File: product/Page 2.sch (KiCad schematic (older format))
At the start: 25 parts, among them J3 Conn_02x05_Odd_Even, Q1 Q_NMOS_GSD, Q2 Q_NMOS_GSD, Q3 Q_NMOS_GSD, SW1 222CMVBAR, SW2 222CMVBAR, U3 ESP32-WROOM-32D, X1 ECS-2520MV

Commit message: Added first revision of programmer board
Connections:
- net labels removed: +5V
- wire segments 98 -> 96
- no-connect marks 19 -> 20
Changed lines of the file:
@@
 Text GLabel 8450 4750 0    50   Input ~ 0
 RESTART
-$Comp
-L Connector_Generic:Conn_02x05_Odd_Even J3
-U 1 1 5DFAE484
-P 5000 6600
-F 0 "J3" H 5050 6925 50  0000 C CNN
-F 1 "Conn_02x05_Odd_Even" H 5050 6926 50  0001 C CNN
-F 2 "Connector_PinSocket_2.54mm:PinSocket_2x05_P2.54mm_Vertical" H 5000 6600 50  0001 C CNN
-F 3 "~" H 5000 6600 50  0001 C CNN
-	1    5000 6600
-	1    0    0    -1
-$EndComp
 Text GLabel 5500 6500 2    50   Input ~ 0
 RX
@@
 L power:GND #PWR0146
 U 1 1 5DFAF37B
-P 4700 6900
-F 0 "#PWR0146" H 4700 6650 50  0001 C CNN
-F 1 "GND" H 4705 6727 50  0000 C CNN
-F 2 "" H 4700 6900 50  0001 C CNN
-F 3 "" H 4700 6900 50  0001 C CNN
-	1    4700 6900
-	1    0    0    -1
-$EndComp
-$Comp
-L power:+5V #PWR0147
-U 1 1 5DFAF73B
-P 4700 6300
-F 0 "#PWR0147" H 4700 6150 50  0001 C CNN
-F 1 "+5V" H 4715 6473 50  0000 C CNN
-F 2 "" H 4700 6300 50  0001 C CNN
-F 3 "" H 4700 6300 50  0001 C CNN
-	1    4700 6300
-	1    0    0    -1
-$EndComp
-Wire Wire Line
-	4800 6400 4700 6400
-Wire Wire Line
-	4700 6400 4700 6300
-Wire Wire Line
-	4800 6800 4700 6800
-Wire Wire Line
-	4700 6800 4700 6900
+P 5400 6900
+F 0 "#PWR0146" H 5400 6650 50  0001 C CNN
+F 1 "GND" H 5405 6727 50  0000 C CNN
+F 2 "" H 5400 6900 50  0001 C CNN
+F 3 "" H 5400 6900 50  0001 C CNN
+	1    5400 6900
+	1    0    0    -1
+$EndComp
+Wire Wire Line
+	5400 6800 5400 6900
 Wire Wire Line
 	5300 6700 5500 6700
@@
 Wire Wire Line
 	5500 6400 5300 6400
-NoConn ~ 5300 6800
 NoConn ~ 4800 6700
 NoConn ~ 4800 6600
@@
 Text GLabel 3850 3200 2    50   Input ~ 0
 CLKEN
+$Comp
+L Connector_Generic:Conn_02x05_Odd_Even J3
+U 1 1 5DFAE484
+P 5000 6600
+F 0 "J3" H 5050 6925 50  0000 C CNN
+F 1 "Conn_02x05_Odd_Even" H 5050 6926 50  0001 C CNN
+F 2 "Connector_PinSocket_2.54mm:PinSocket_2x05_P2.54mm_Vertical" H 5000 6600 50  0001 C CNN
+F 3 "~" H 5000 6600 50  0001 C CNN
+	1    5000 6600
+	1    0    0    -1
+$EndComp
+Wire Wire Line
+	5300 6800 5400 6800
+NoConn ~ 4800 6800
+NoConn ~ 4800 6400
 $EndSCHEMATC

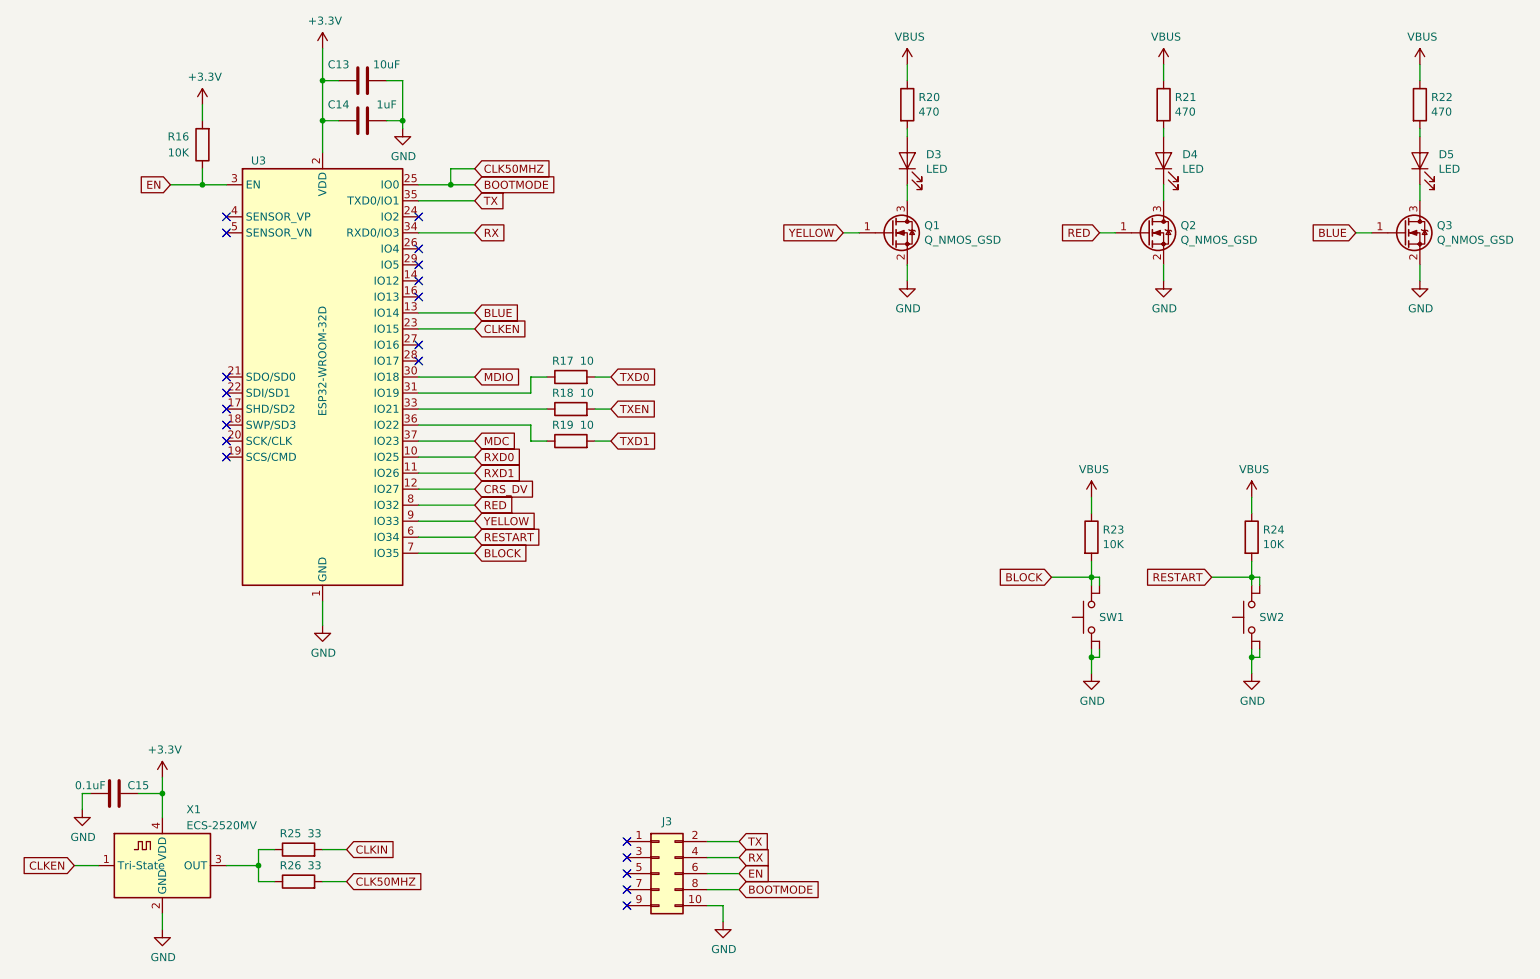
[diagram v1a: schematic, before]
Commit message: Added LCSC part numbers for product board
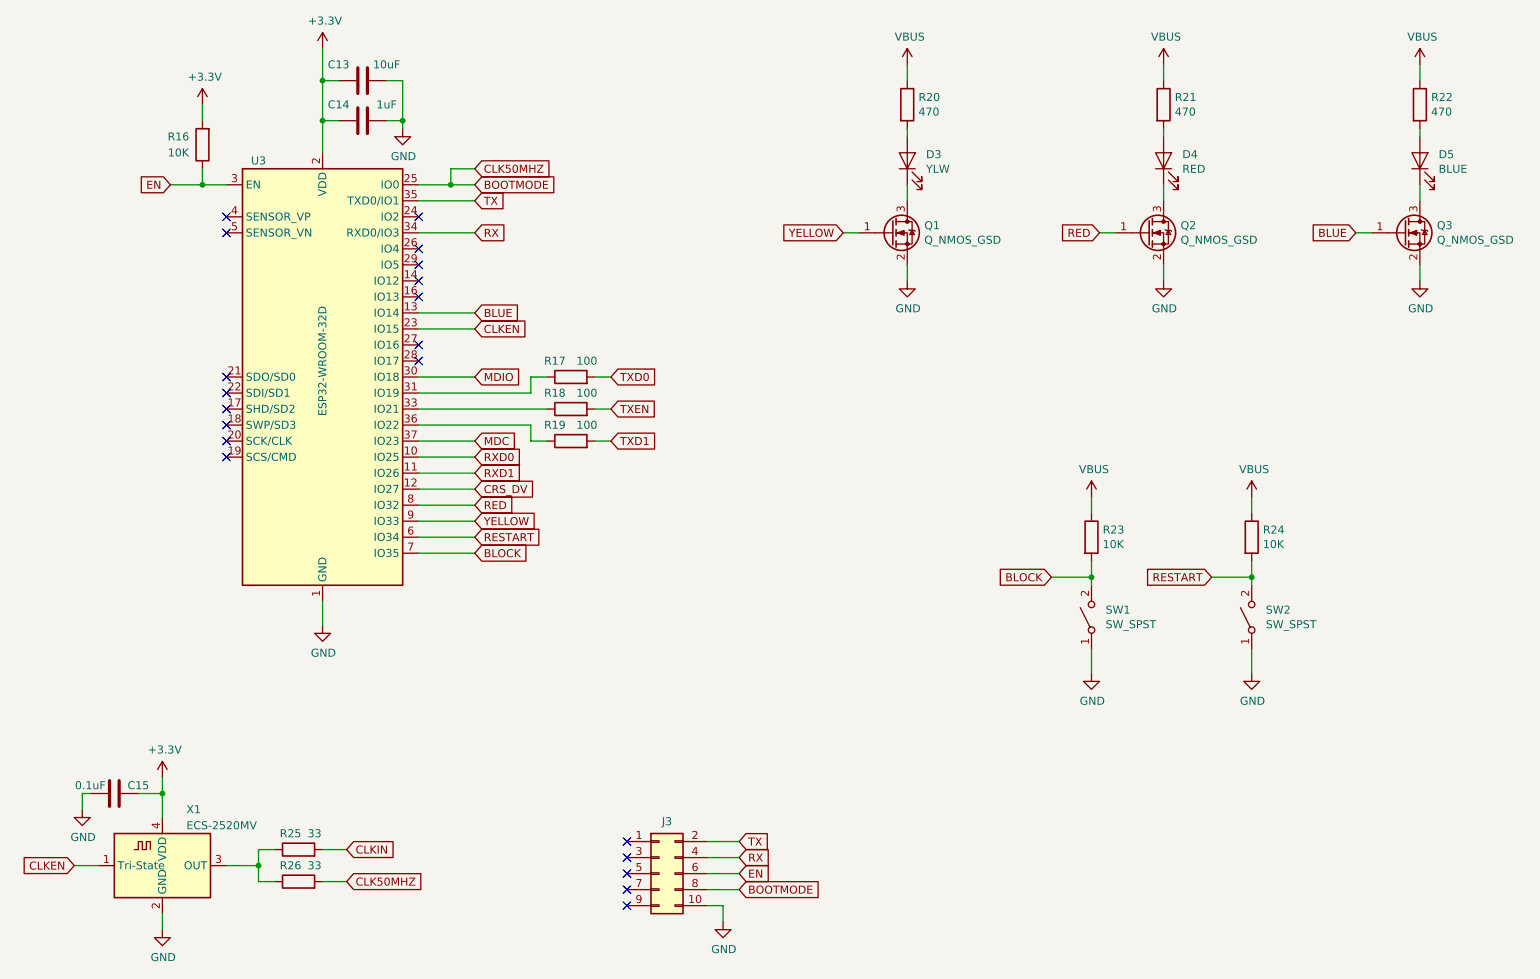
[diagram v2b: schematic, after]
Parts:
- removed SW1, SW2: 222CMVBAR, My Footprints:222CMVBAR, symbol My_Symbols:222CMVBAR
- added SW1, SW2: SW_SPST, Button_Switch_SMD:SW_Push_1P1T_NO_6x6mm_H9.5mm, symbol Switch:SW_SPST
- C13: LCSC Part Number (none) -> C77044
- C14: LCSC Part Number (none) -> C1525
- C15: LCSC Part Number (none) -> C24452
- D3: value LED -> YLW; LCSC Part Number (none) -> C125101
- D4: value LED -> RED; LCSC Part Number (none) -> C125099
- D5: value LED -> BLUE; LCSC Part Number (none) -> C99290
- Q1, Q2, Q3: LCSC Part Number (none) -> C71533
- R16, R23, R24: LCSC Part Number (none) -> C99198
- R17, R18, R19: value 10 -> 100; LCSC Part Number (none) -> C105588
- R20, R21, R22: LCSC Part Number (none) -> C114433
- R25, R26: LCSC Part Number (none) -> C417099
- U3: LCSC Part Number (none) -> C95209
- X1: LCSC Part Number (none) -> C405472
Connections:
- net BLOCK: now also SW1.2 (B)
- net GND: now also SW1.1 (A), SW2.1 (A)
- net RESTART: now also SW2.2 (B)
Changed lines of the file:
@@
 EESchema Schematic File Version 4
-LIBS:EsperDNS-cache
 EELAYER 30 0
 EELAYER END
@@
 F 2 "Oscillator:Oscillator_SMD_ECS_2520MV-xxx-xx-4Pin_2.5x2.0mm" H 2350 6200 50  0001 C CNN
 F 3 "https://www.ecsxtal.com/store/pdf/ECS-2520MV.pdf" H 1725 6675 50  0001 C CNN
+F 4 " C405472" H 1900 6550 50  0001 C CNN "LCSC Part Number"
 	1    1900 6550
 	1    0    0    -1
@@
 F 2 "RF_Module:ESP32-WROOM-32" H 2900 2000 50  0001 C CNN
 F 3 "https://www.espressif.com/sites/default/files/documentation/esp32-wroom-32d_esp32-wroom-32u_datasheet_en.pdf" H 2600 3550 50  0001 C CNN
+F 4 " 	C95209" H 2900 3500 50  0001 C CNN "LCSC Part Number"
 	1    2900 3500
 	1    0    0    -1
@@
 U 1 1 5DF2BBCB
 P 4450 3700
-F 0 "R18" V 4550 3750 50  0000 C CNN
-F 1 "10" V 4550 3600 50  0000 C CNN
+F 0 "R18" V 4550 3800 50  0000 C CNN
+F 1 "100" V 4550 3600 50  0000 C CNN
 F 2 "Resistor_SMD:R_0603_1608Metric" V 4380 3700 50  0001 C CNN
 F 3 "~" H 4450 3700 50  0001 C CNN
+F 4 "C105588" H 4450 3700 50  0001 C CNN "LCSC Part Number"
 	1    4450 3700
 	0    -1   -1   0
@@
 U 1 1 5DF2BD63
 P 4450 3900
-F 0 "R19" V 4550 3950 50  0000 C CNN
-F 1 "10" V 4550 3800 50  0000 C CNN
+F 0 "R19" V 4550 4000 50  0000 C CNN
+F 1 "100" V 4550 3800 50  0000 C CNN
 F 2 "Resistor_SMD:R_0603_1608Metric" V 4380 3900 50  0001 C CNN
 F 3 "~" H 4450 3900 50  0001 C CNN
+F 4 "C105588" H 4450 3900 50  0001 C CNN "LCSC Part Number"
 	1    4450 3900
 	0    -1   -1   0
@@
 F 2 "Capacitor_SMD:C_0603_1608Metric" H 3188 1750 50  0001 C CNN
 F 3 "~" H 3150 1900 50  0001 C CNN
+F 4 "C1525" H 3150 1900 50  0001 C CNN "LCSC Part Number"
 	1    3150 1900
 	0    1    1    0
@@
 F 2 "Capacitor_SMD:C_0603_1608Metric" H 3188 1500 50  0001 C CNN
 F 3 "~" H 3150 1650 50  0001 C CNN
+F 4 "C77044" H 3150 1650 50  0001 C CNN "LCSC Part Number"
 	1    3150 1650
 	0    1    1    0
@@
 F 2 "Resistor_SMD:R_0603_1608Metric" V 2080 2050 50  0001 C CNN
 F 3 "~" H 2150 2050 50  0001 C CNN
+F 4 "C99198" H 2150 2050 50  0001 C CNN "LCSC Part Number"
 	1    2150 2050
 	-1   0    0    1
@@
 U 1 1 5DF2A186
 P 4450 3500
-F 0 "R17" V 4550 3550 50  0000 C CNN
-F 1 "10" V 4550 3400 50  0000 C CNN
+F 0 "R17" V 4550 3600 50  0000 C CNN
+F 1 "100" V 4550 3400 50  0000 C CNN
 F 2 "Resistor_SMD:R_0603_1608Metric" V 4380 3500 50  0001 C CNN
 F 3 "~" H 4450 3500 50  0001 C CNN
+F 4 "C105588" H 4450 3500 50  0001 C CNN "LCSC Part Number"
 	1    4450 3500
 	0    -1   -1   0
@@
 AR Path="/5DED3446/5DF435C4" Ref="D5"  Part="1"
 F 0 "D5" V 9789 2033 50  0000 R CNN
-F 1 "LED" V 9698 2033 50  0000 R CNN
+F 1 "BLUE" V 9698 2033 50  0000 R CNN
 F 2 "Diode_SMD:D_0603_1608Metric" H 9750 2150 50  0001 C CNN
 F 3 "~" H 9750 2150 50  0001 C CNN
+F 4 "C99290" H 9750 2150 50  0001 C CNN "LCSC Part Number"
 	1    9750 2150
 	0    -1   -1   0
@@
 F 2 "digikey-footprints:SOT-23-3" H 9850 2700 50  0001 C CNN
 F 3 "~" H 9650 2600 50  0001 C CNN
+F 4 "C71533" H 9650 2600 50  0001 C CNN "LCSC Part Number"
 	1    9650 2600
 	1    0    0    -1
@@
 AR Path="/5DED3446/5DF5064C" Ref="D4"  Part="1"
 F 0 "D4" V 8189 2033 50  0000 R CNN
-F 1 "LED" V 8098 2033 50  0000 R CNN
+F 1 "RED" V 8098 2033 50  0000 R CNN
 F 2 "Diode_SMD:D_0603_1608Metric" H 8150 2150 50  0001 C CNN
 F 3 "~" H 8150 2150 50  0001 C CNN
+F 4 "C125099" H 8150 2150 50  0001 C CNN "LCSC Part Number"
 	1    8150 2150
 	0    -1   -1   0
@@
 F 2 "digikey-footprints:SOT-23-3" H 8250 2700 50  0001 C CNN
 F 3 "~" H 8050 2600 50  0001 C CNN
+F 4 "C71533" H 8050 2600 50  0001 C CNN "LCSC Part Number"
 	1    8050 2600
 	1    0    0    -1
@@
 AR Path="/5DED3446/5DF52B0B" Ref="D3"  Part="1"
 F 0 "D3" V 6589 2033 50  0000 R CNN
-F 1 "LED" V 6498 2033 50  0000 R CNN
+F 1 "YLW" V 6498 2033 50  0000 R CNN
 F 2 "Diode_SMD:D_0603_1608Metric" H 6550 2150 50  0001 C CNN
 F 3 "~" H 6550 2150 50  0001 C CNN
+F 4 "C125101" H 6550 2150 50  0001 C CNN "LCSC Part Number"
 	1    6550 2150
 	0    -1   -1   0
@@
 F 2 "digikey-footprints:SOT-23-3" H 6650 2700 50  0001 C CNN
 F 3 "~" H 6450 2600 50  0001 C CNN
+F 4 "C71533" H 6450 2600 50  0001 C CNN "LCSC Part Number"
 	1    6450 2600
 	1    0    0    -1
@@
 F 2 "Resistor_SMD:R_0603_1608Metric" V 2680 6450 50  0001 C CNN
 F 3 "~" H 2750 6450 50  0001 C CNN
+F 4 "C417099" H 2750 6450 50  0001 C CNN "LCSC Part Number"
 	1    2750 6450
 	0    -1   -1   0
@@
 F 2 "Resistor_SMD:R_0603_1608Metric" V 2680 6650 50  0001 C CNN
 F 3 "~" H 2750 6650 50  0001 C CNN
+F 4 "C417099" H 2750 6650 50  0001 C CNN "LCSC Part Number"
 	1    2750 6650
 	0    -1   -1   0
@@
 F 2 "Resistor_SMD:R_0603_1608Metric" V 7630 4500 50  0001 C CNN
 F 3 "~" H 7700 4500 50  0001 C CNN
+F 4 "C99198" H 7700 4500 50  0001 C CNN "LCSC Part Number"
 	1    7700 4500
 	1    0    0    -1
@@
 Wire Wire Line
 	7700 4650 7700 4750
-Wire Wire Line
-	7700 5350 7700 5250
 Text GLabel 7450 4750 0    50   Input ~ 0
 BLOCK
@@
 F 2 "Resistor_SMD:R_0603_1608Metric" V 8630 4500 50  0001 C CNN
 F 3 "~" H 8700 4500 50  0001 C CNN
+F 4 "C99198" H 8700 4500 50  0001 C CNN "LCSC Part Number"
 	1    8700 4500
 	1    0    0    -1
@@
 Wire Wire Line
 	8700 4650 8700 4750
-Wire Wire Line
-	8700 5350 8700 5250
 Text GLabel 8450 4750 0    50   Input ~ 0
 RESTART
@@
 F 2 "Capacitor_SMD:C_0603_1608Metric" H 1638 5950 50  0001 C CNN
 F 3 "~" H 1600 6100 50  0001 C CNN
+F 4 "C24452" H 1600 6100 50  0001 C CNN "LCSC Part Number"
 	1    1600 6100
 	0    -1   -1   0
@@
 Wire Wire Line
 	1400 6100 1400 6200
-$Comp
-L My_Symbols:222CMVBAR SW1
-U 1 1 5DFB5FF6
-P 7700 5000
-F 0 "SW1" V 7700 4952 50  0000 R CNN
-F 1 "222CMVBAR" V 7655 4952 50  0001 R CNN
-F 2 "My Footprints:222CMVBAR" H 7700 5200 50  0001 C CNN
-F 3 "~" H 7700 5200 50  0001 C CNN
-	1    7700 5000
-	0    -1   -1   0
-$EndComp
-$Comp
-L My_Symbols:222CMVBAR SW2
-U 1 1 5DFB7206
-P 8700 5000
-F 0 "SW2" V 8700 4952 50  0000 R CNN
-F 1 "222CMVBAR" V 8655 4952 50  0001 R CNN
-F 2 "My Footprints:222CMVBAR" H 8700 5200 50  0001 C CNN
-F 3 "~" H 8700 5200 50  0001 C CNN
-	1    8700 5000
-	0    -1   -1   0
-$EndComp
-Wire Wire Line
-	7750 5200 7750 5250
-Wire Wire Line
-	7750 5250 7700 5250
-Connection ~ 7700 5250
-Wire Wire Line
-	7700 5250 7700 5200
-Wire Wire Line
-	7750 4800 7750 4750
-Wire Wire Line
-	7750 4750 7700 4750
-Wire Wire Line
-	8750 4800 8750 4750
-Wire Wire Line
-	8750 4750 8700 4750
-Wire Wire Line
-	8750 5200 8750 5250
-Wire Wire Line
-	8750 5250 8700 5250
-Connection ~ 8700 5250
-Wire Wire Line
-	8700 5250 8700 5200
 $Comp
 L power:VBUS #PWR?
@@
 F 2 "Resistor_SMD:R_0603_1608Metric" V 9680 1800 50  0001 C CNN
 F 3 "~" H 9750 1800 50  0001 C CNN
+F 4 "C114433" H 9750 1800 50  0001 C CNN "LCSC Part Number"
 	1    9750 1800
 	1    0    0    -1
@@
 F 2 "Resistor_SMD:R_0603_1608Metric" V 8080 1800 50  0001 C CNN
 F 3 "~" H 8150 1800 50  0001 C CNN
+F 4 "C114433" H 8150 1800 50  0001 C CNN "LCSC Part Number"
 	1    8150 1800
 	1    0    0    -1
@@
 F 2 "Resistor_SMD:R_0603_1608Metric" V 6480 1800 50  0001 C CNN
 F 3 "~" H 6550 1800 50  0001 C CNN
+F 4 "C114433" H 6550 1800 50  0001 C CNN "LCSC Part Number"
 	1    6550 1800
 	1    0    0    -1
@@
 NoConn ~ 4800 6800
 NoConn ~ 4800 6400
+Wire Wire Line
+	8700 5200 8700 5350
+Wire Wire Line
+	7700 5200 7700 5350
+$Comp
+L Switch:SW_SPST SW1
+U 1 1 5DF79310
+P 7700 5000
+F 0 "SW1" V 7746 4912 50  0000 R CNN
+F 1 "SW_SPST" V 7655 4912 50  0000 R CNN
+F 2 "Button_Switch_SMD:SW_Push_1P1T_NO_6x6mm_H9.5mm" H 7700 5000 50  0001 C CNN
+F 3 "~" H 7700 5000 50  0001 C CNN
+F 4 "C221880" H 7700 5000 50  0001 C CNN "LCSC Part Number"
+	1    7700 5000
+	0    -1   -1   0
+$EndComp
+$Comp
+L Switch:SW_SPST SW2
+U 1 1 5DF79D9C
+P 8700 5000
+F 0 "SW2" V 8746 4912 50  0000 R CNN
+F 1 "SW_SPST" V 8655 4912 50  0000 R CNN
+F 2 "Button_Switch_SMD:SW_Push_1P1T_NO_6x6mm_H9.5mm" H 8700 5000 50  0001 C CNN
+F 3 "~" H 8700 5000 50  0001 C CNN
+F 4 "C221880" H 8700 5000 50  0001 C CNN "LCSC Part Number"
+	1    8700 5000
+	0    -1   -1   0
+$EndComp
 $EndSCHEMATC

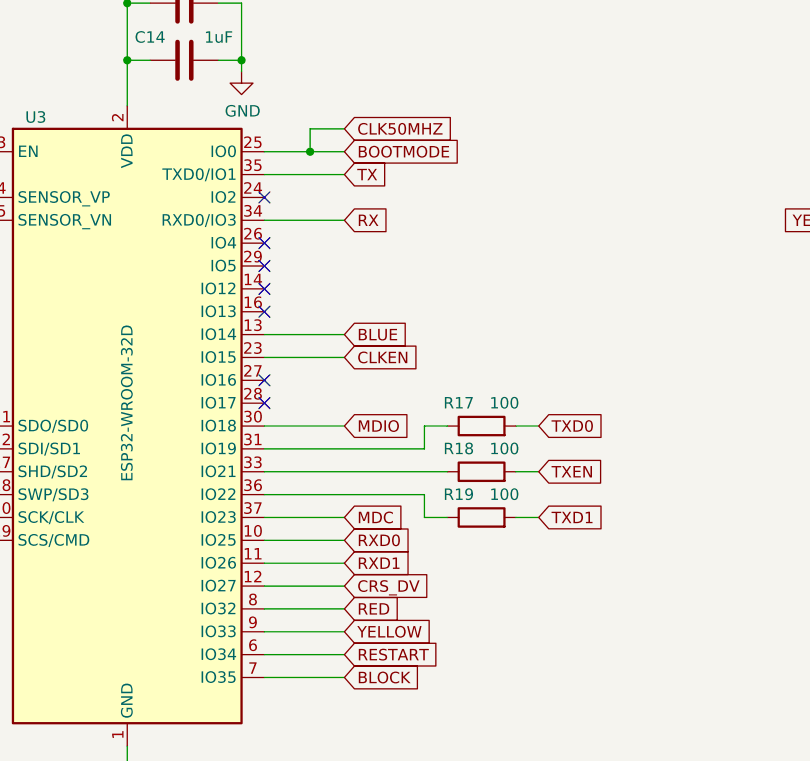
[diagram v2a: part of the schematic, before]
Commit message: Swapped TX & RX on Product Board
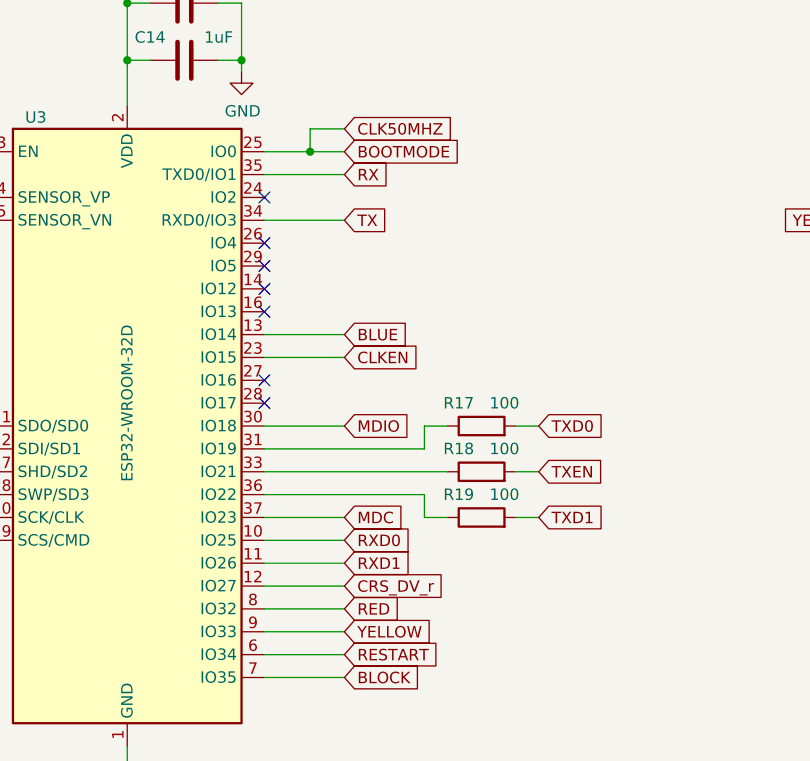
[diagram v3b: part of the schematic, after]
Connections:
- net RX: now also U3.35 (TXD0/IO1); no longer U3.34 (RXD0/IO3)
- net TX: now also U3.34 (RXD0/IO3); no longer U3.35 (TXD0/IO1)
- net CRS_DV renamed CRS_DV_r
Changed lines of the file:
@@
 MDIO
 Text GLabel 3850 4200 2    50   Input ~ 0
-CRS_DV
+CRS_DV_r
 Text GLabel 3850 4100 2    50   Input ~ 0
 RXD1
@@
 CLKIN
 Text GLabel 3850 2400 2    50   Input ~ 0
+RX
+Text GLabel 3850 2600 2    50   Input ~ 0
 TX
-Text GLabel 3850 2600 2    50   Input ~ 0
-RX
 Text GLabel 3850 2300 2    50   Input ~ 0
 BOOTMODE
